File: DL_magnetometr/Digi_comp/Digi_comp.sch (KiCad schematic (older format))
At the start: 30 parts, among them J1 USB_B_Micro, U1 AP7331-WG-7, U2 74AHCT1G125, U3 JST-PHR-2, U4 AZ4558CM, U5 AZ4558CM

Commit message: Add files via upload
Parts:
- added C10, C7, C8, C9: 100n, Capacitor_SMD:C_0402_1005Metric, symbol Device:C
- added C11: 8.2p, Capacitor_SMD:C_0402_1005Metric, symbol Device:C
- added C12, C13: 1.8p, symbol Device:C
- added C14: 0.1u, Capacitor_SMD:C_0402_1005Metric, symbol Device:C
- added C15, C16: 1u, symbol Device:C
- added C4: 4.7u, symbol Device:C
- added L1: 3.3n, symbol Device:L
- added Y1: 32.768k, symbol Device:Crystal
- added Y2: 16M/32M, symbol Device:Crystal
- B1: renamed from B?; symbol RF_Bluetooth:QN908x -> Digi_comp-rescue:QN908x-RF_Bluetooth
- S1: renamed from S?; symbol Sensor:HMC5883L -> Digi_comp-rescue:HMC5883L-Sensor
- U1: symbol Regulator_Linear:AP7331-WG-7 -> Digi_comp-rescue:AP7331-WG-7-Regulator_Linear
- U3: symbol Connector:JST-PHR-2 -> Digi_comp-rescue:JST-PHR-2-Connector
- U4, U5: symbol Amplifier_Audio:AZ4558CM -> Digi_comp-rescue:AZ4558CM-Amplifier_Audio
- U6: renamed from U?; symbol Regulator_Linear:AP7331-WG-7 -> Digi_comp-rescue:AP7331-WG-7-Regulator_Linear
- gave numbers to parts that had none: 1
- renumbered RG to RG1, R_SHUNT to R_SHUNT1
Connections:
- net labels added: CHIP_MODE, ISP_RXD, ISP_TXD, RSTN, SW_CLK, SW_DIO
- wire segments 113 -> 172
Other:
- note added: "#ToDo: Antenna"
- note added: "#Todo: Fix RESET bug\n"
- moved on the sheet: R11, R12, R13

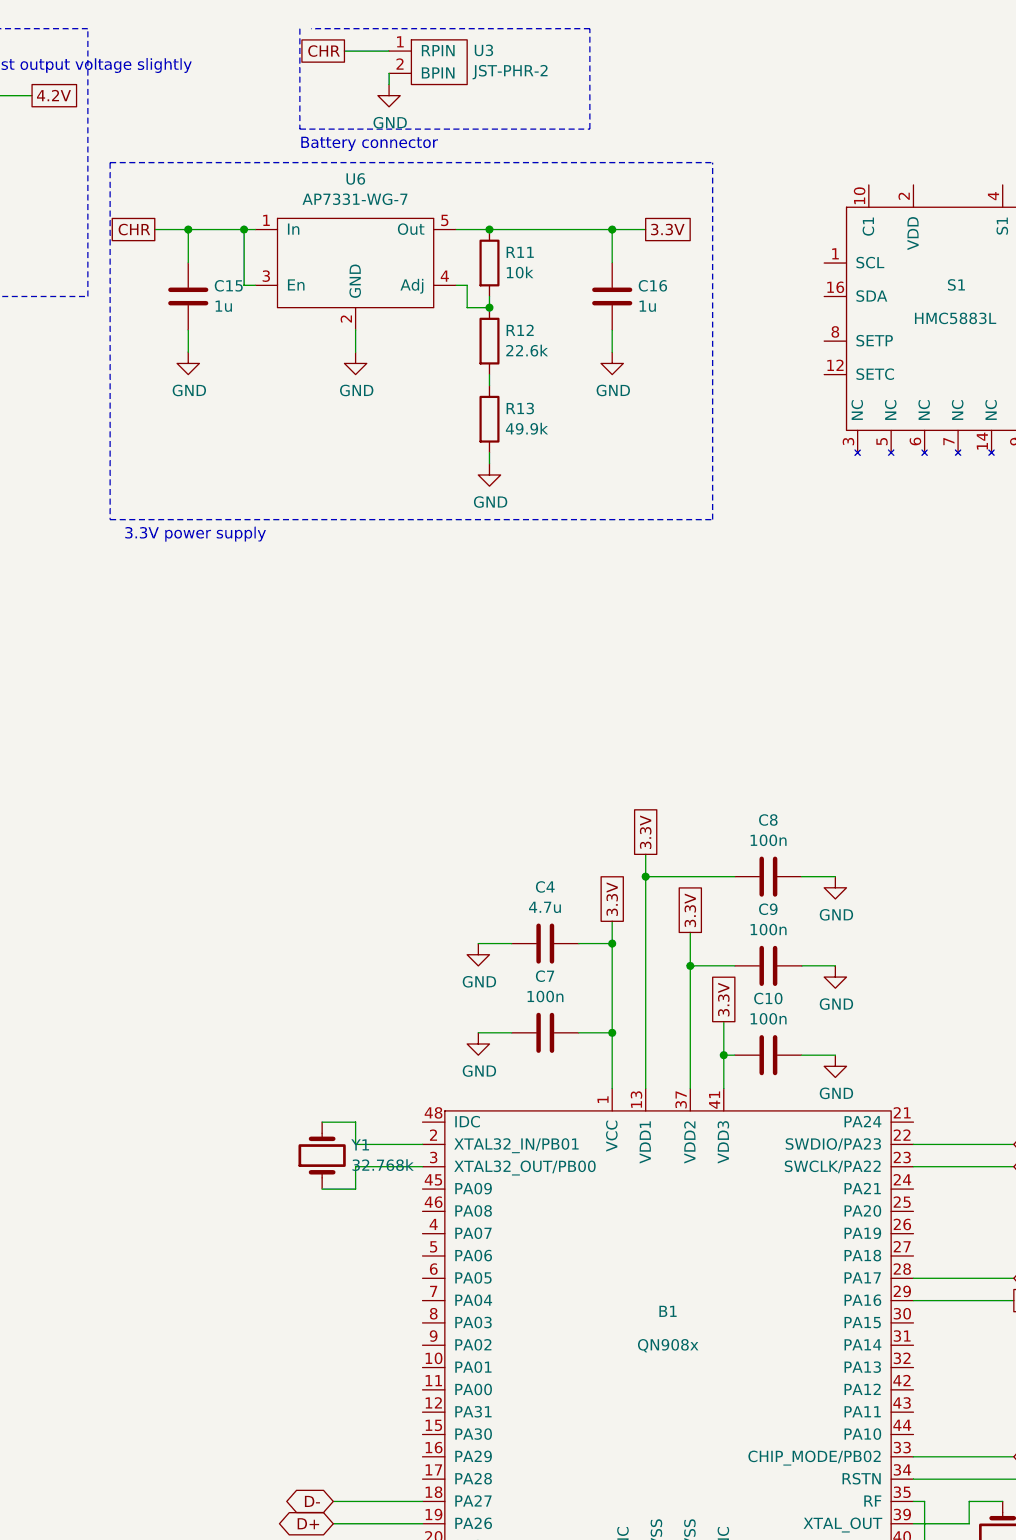
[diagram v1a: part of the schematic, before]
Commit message: Modified scheme
Now utilising on-chip DC-DC converter for lower power consumption. Added overcurrent protection fuses.
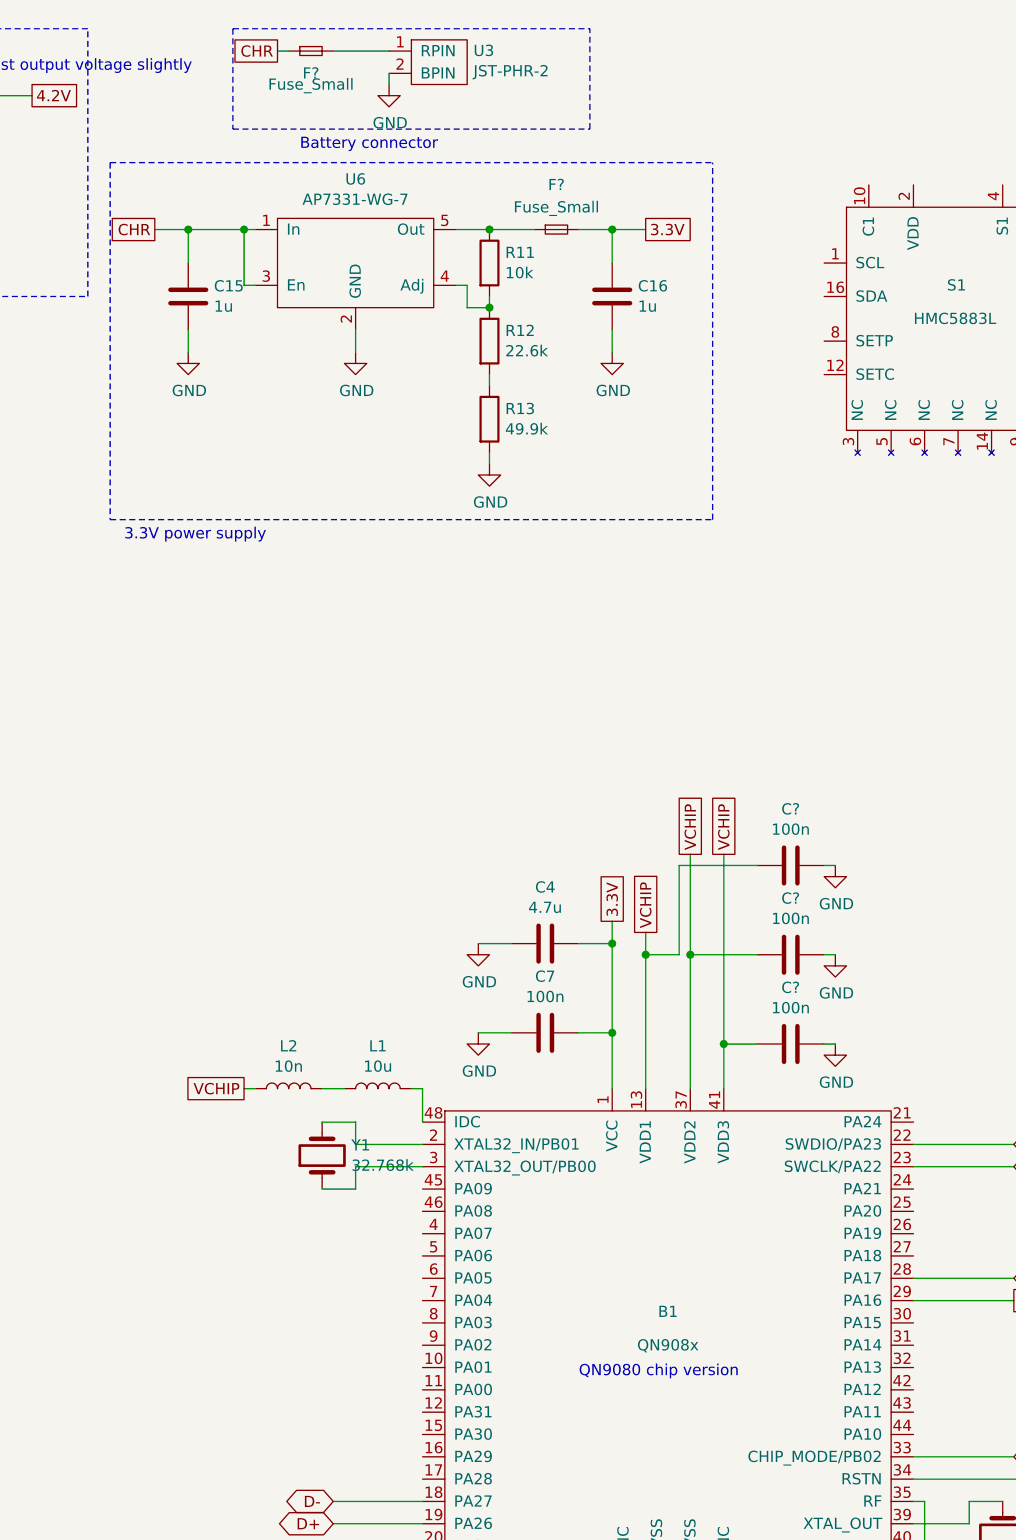
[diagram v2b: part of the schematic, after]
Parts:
- removed C10, C8, C9: 100n, Capacitor_SMD:C_0402_1005Metric, symbol Device:C
- added C? (x3): 100n, Capacitor_SMD:C_0402_1005Metric, symbol Device:C
- added F? (x2): Fuse_Small, symbol Device:Fuse_Small
- added L1: 10u, symbol Device:L
- added L2: 10n, symbol Device:L
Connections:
- net 3.3V: now also F?.2; no longer B1.13 (VDD1), B1.37 (VDD2), B1.41 (VDD3), R11.1, U6.5 (Out)
- net CHR: now also F?.1; no longer U3.1 (RPIN)
- net GND: now also C?.1, C?.1, C?.1
- net at B1.48 (IDC): now also L1.2
- new net: F?.2, U3.1 (RPIN)
- new net: F?.1, R11.1, U6.5 (Out)
- new net: L1.1, L2.2
- new net VCHIP: B1.13 (VDD1), B1.37 (VDD2), B1.41 (VDD3), C?.2, C?.2, C?.2, L2.1
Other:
- note added: "QN9080 chip version"
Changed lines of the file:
@@
 Text GLabel 2200 4900 2    50   UnSpc ~ 0
 BAT
-Wire Wire Line
-	6500 700  6300 700
 $Comp
 L Digi_comp-rescue:AZ4558CM-Amplifier_Audio U4
@@
 Text GLabel 1600 4900 0    50   UnSpc ~ 0
 CHR
-Text GLabel 6300 700  0    50   UnSpc ~ 0
+Text GLabel 6000 700  0    50   UnSpc ~ 0
 CHR
 Text Notes 4050 800  0    50   ~ 0
@@
 $EndComp
 Wire Notes Line
-	6100 600  6100 1050
-Wire Notes Line
-	6100 1050 7400 1050
+	5800 600  5800 1050
 Wire Notes Line
 	7400 1050 7400 600
-Wire Notes Line
-	7400 600  6150 600
 Text Notes 6100 1150 0    50   ~ 0
 Battery connector
@@
 Text GLabel 7650 1500 2    50   UnSpc ~ 0
 3.3V
-Connection ~ 6950 1500
 Wire Wire Line
 	1450 2750 1100 2750
@@
 Wire Wire Line
 	6900 4700 7050 4700
-$Comp
-L Device:C C10
-U 1 1 5FDD7B44
-P 8200 5200
-F 0 "C10" V 7948 5200 50  0000 C CNN
-F 1 "100n" V 8039 5200 50  0000 C CNN
-F 2 "Capacitor_SMD:C_0402_1005Metric" H 8238 5050 50  0001 C CNN
-F 3 "~" H 8200 5200 50  0001 C CNN
-	1    8200 5200
-	0    1    1    0
-$EndComp
-$Comp
-L power:GND #PWR03
-U 1 1 5FDD8027
-P 8500 5200
-F 0 "#PWR03" H 8500 4950 50  0001 C CNN
-F 1 "GND" H 8505 5027 50  0000 C CNN
-F 2 "" H 8500 5200 50  0001 C CNN
-F 3 "" H 8500 5200 50  0001 C CNN
-	1    8500 5200
-	1    0    0    -1
-$EndComp
-$Comp
-L Device:C C9
-U 1 1 5FDD8471
-P 8200 4800
-F 0 "C9" V 7948 4800 50  0000 C CNN
-F 1 "100n" V 8039 4800 50  0000 C CNN
-F 2 "Capacitor_SMD:C_0402_1005Metric" H 8238 4650 50  0001 C CNN
-F 3 "~" H 8200 4800 50  0001 C CNN
-	1    8200 4800
-	0    1    1    0
-$EndComp
-$Comp
-L power:GND #PWR02
-U 1 1 5FDD87FC
-P 8500 4800
-F 0 "#PWR02" H 8500 4550 50  0001 C CNN
-F 1 "GND" H 8505 4627 50  0000 C CNN
-F 2 "" H 8500 4800 50  0001 C CNN
-F 3 "" H 8500 4800 50  0001 C CNN
-	1    8500 4800
-	1    0    0    -1
-$EndComp
-Text GLabel 8000 5050 1    50   UnSpc ~ 0
-3.3V
-Text GLabel 7850 4650 1    50   UnSpc ~ 0
-3.3V
-$Comp
-L Device:C C8
-U 1 1 5FDDA27E
-P 8200 4400
-F 0 "C8" V 7948 4400 50  0000 C CNN
-F 1 "100n" V 8039 4400 50  0000 C CNN
-F 2 "Capacitor_SMD:C_0402_1005Metric" H 8238 4250 50  0001 C CNN
-F 3 "~" H 8200 4400 50  0001 C CNN
-	1    8200 4400
-	0    1    1    0
-$EndComp
-$Comp
-L power:GND #PWR01
-U 1 1 5FDDAA82
-P 8500 4400
-F 0 "#PWR01" H 8500 4150 50  0001 C CNN
-F 1 "GND" H 8505 4227 50  0000 C CNN
-F 2 "" H 8500 4400 50  0001 C CNN
-F 3 "" H 8500 4400 50  0001 C CNN
-	1    8500 4400
-	1    0    0    -1
-$EndComp
-Text GLabel 7650 4300 1    50   UnSpc ~ 0
-3.3V
-Wire Wire Line
-	8350 4400 8500 4400
-Wire Wire Line
-	8350 4800 8500 4800
-Wire Wire Line
-	7650 4300 7650 4400
-Wire Wire Line
-	7850 4650 7850 4800
-Wire Wire Line
-	7650 4400 8050 4400
-Wire Wire Line
-	7850 4800 8050 4800
-Wire Wire Line
-	8050 5200 8000 5200
-Wire Wire Line
-	8000 5200 8000 5050
-Wire Wire Line
-	8000 5200 8000 5350
-Connection ~ 8000 5200
-Wire Wire Line
-	8350 5200 8500 5200
 Text GLabel 9300 6300 2    50   Output ~ 0
 ISP_TXD
@@
 Text GLabel 6250 7200 0    50   BiDi ~ 0
 D-
-Wire Wire Line
-	7850 5350 7850 4800
-Connection ~ 7850 4800
-Wire Wire Line
-	7650 5350 7650 4400
-Connection ~ 7650 4400
 Text Notes 8750 8700 0    50   ~ 0
 #ToDo: Antenna
@@
 	7500 1500 7650 1500
 Wire Wire Line
-	6950 1500 7500 1500
-Connection ~ 7500 1500
-Wire Wire Line
 	5450 1500 5600 1500
 Wire Wire Line
@@
 Wire Notes Line
 	5250 2800 7950 2800
+$Comp
+L Device:Fuse_Small F?
+U 1 1 5FD84E19
+P 6150 700
+F 0 "F?" H 6150 600 50  0000 C CNN
+F 1 "Fuse_Small" H 6150 550 50  0000 C CNN
+F 2 "" H 6150 700 50  0001 C CNN
+F 3 "~" H 6150 700 50  0001 C CNN
+	1    6150 700
+	1    0    0    -1
+$EndComp
+Wire Wire Line
+	6250 700  6500 700
+Wire Wire Line
+	6050 700  6000 700
+Wire Notes Line
+	5800 1050 7400 1050
+Wire Notes Line
+	5800 600  7400 600
+$Comp
+L Device:Fuse_Small F?
+U 1 1 5FDB2E3B
+P 7250 1500
+F 0 "F?" H 7250 1700 50  0000 C CNN
+F 1 "Fuse_Small" H 7250 1600 50  0000 C CNN
+F 2 "" H 7250 1500 50  0001 C CNN
+F 3 "~" H 7250 1500 50  0001 C CNN
+	1    7250 1500
+	1    0    0    -1
+$EndComp
+Wire Wire Line
+	6950 1500 7150 1500
+Connection ~ 6950 1500
+Wire Wire Line
+	7350 1500 7500 1500
+Connection ~ 7500 1500
+$Comp
+L Device:L L1
+U 1 1 5FDC3994
+P 6450 5350
+F 0 "L1" V 6640 5350 50  0000 C CNN
+F 1 "10u" V 6549 5350 50  0000 C CNN
+F 2 "" H 6450 5350 50  0001 C CNN
+F 3 "~" H 6450 5350 50  0001 C CNN
+	1    6450 5350
+	0    -1   -1   0
+$EndComp
+$Comp
+L Device:L L2
+U 1 1 5FDC45C3
+P 6050 5350
+F 0 "L2" V 6240 5350 50  0000 C CNN
+F 1 "10n" V 6149 5350 50  0000 C CNN
+F 2 "" H 6050 5350 50  0001 C CNN
+F 3 "~" H 6050 5350 50  0001 C CNN
+	1    6050 5350
+	0    -1   -1   0
+$EndComp
+Wire Wire Line
+	6650 5500 6650 5350
+Wire Wire Line
+	6650 5350 6600 5350
+Wire Wire Line
+	6300 5350 6200 5350
+Text GLabel 5850 5350 0    50   UnSpc ~ 0
+VCHIP
+Wire Wire Line
+	5900 5350 5850 5350
+Text GLabel 7650 4650 1    50   UnSpc ~ 0
+VCHIP
+$Comp
+L Device:C C?
+U 1 1 5FDDA059
+P 8300 4750
+F 0 "C?" V 8048 4750 50  0000 C CNN
+F 1 "100n" V 8139 4750 50  0000 C CNN
+F 2 "Capacitor_SMD:C_0402_1005Metric" H 8338 4600 50  0001 C CNN
+F 3 "~" H 8300 4750 50  0001 C CNN
+	1    8300 4750
+	0    1    1    0
+$EndComp
+$Comp
+L Device:C C?
+U 1 1 5FDDAC74
+P 8300 5150
+F 0 "C?" V 8048 5150 50  0000 C CNN
+F 1 "100n" V 8139 5150 50  0000 C CNN
+F 2 "Capacitor_SMD:C_0402_1005Metric" H 8338 5000 50  0001 C CNN
+F 3 "~" H 8300 5150 50  0001 C CNN
+	1    8300 5150
+	0    1    1    0
+$EndComp
+$Comp
+L Device:C C?
+U 1 1 5FDDB25A
+P 8300 4350
+F 0 "C?" V 8048 4350 50  0000 C CNN
+F 1 "100n" V 8139 4350 50  0000 C CNN
+F 2 "Capacitor_SMD:C_0402_1005Metric" H 8338 4200 50  0001 C CNN
+F 3 "~" H 8300 4350 50  0001 C CNN
+	1    8300 4350
+	0    1    1    0
+$EndComp
+Wire Wire Line
+	7650 4650 7650 4750
+Wire Wire Line
+	7650 4750 7800 4750
+Wire Wire Line
+	7800 4750 7800 4350
+Wire Wire Line
+	7800 4350 8150 4350
+Connection ~ 7650 4750
+Wire Wire Line
+	7650 4750 7650 5350
+Text GLabel 7850 4300 1    50   UnSpc ~ 0
+VCHIP
+Wire Wire Line
+	7850 4300 7850 4750
+Wire Wire Line
+	7850 4750 8150 4750
+Connection ~ 7850 4750
+Wire Wire Line
+	7850 4750 7850 5350
+Text GLabel 8000 4300 1    50   UnSpc ~ 0
+VCHIP
+Wire Wire Line
+	8000 4300 8000 5150
+Wire Wire Line
+	8150 5150 8000 5150
+Connection ~ 8000 5150
+Wire Wire Line
+	8000 5150 8000 5350
+$Comp
+L power:GND #PWR?
+U 1 1 5FE096DE
+P 8500 5150
+F 0 "#PWR?" H 8500 4900 50  0001 C CNN
+F 1 "GND" H 8505 4977 50  0000 C CNN
+F 2 "" H 8500 5150 50  0001 C CNN
+F 3 "" H 8500 5150 50  0001 C CNN
+	1    8500 5150
+	1    0    0    -1
+$EndComp
+Wire Wire Line
+	8500 5150 8450 5150
+$Comp
+L power:GND #PWR?
+U 1 1 5FE11A43
+P 8500 4750
+F 0 "#PWR?" H 8500 4500 50  0001 C CNN
+F 1 "GND" H 8505 4577 50  0000 C CNN
+F 2 "" H 8500 4750 50  0001 C CNN
+F 3 "" H 8500 4750 50  0001 C CNN
+	1    8500 4750
+	1    0    0    -1
+$EndComp
+Wire Wire Line
+	8500 4750 8450 4750
+$Comp
+L power:GND #PWR?
+U 1 1 5FE1A0CD
+P 8500 4350
+F 0 "#PWR?" H 8500 4100 50  0001 C CNN
+F 1 "GND" H 8505 4177 50  0000 C CNN
+F 2 "" H 8500 4350 50  0001 C CNN
+F 3 "" H 8500 4350 50  0001 C CNN
+	1    8500 4350
+	1    0    0    -1
+$EndComp
+Wire Wire Line
+	8500 4350 8450 4350
+Text Notes 7350 6650 0    50   ~ 0
+QN9080 chip version
 $EndSCHEMATC

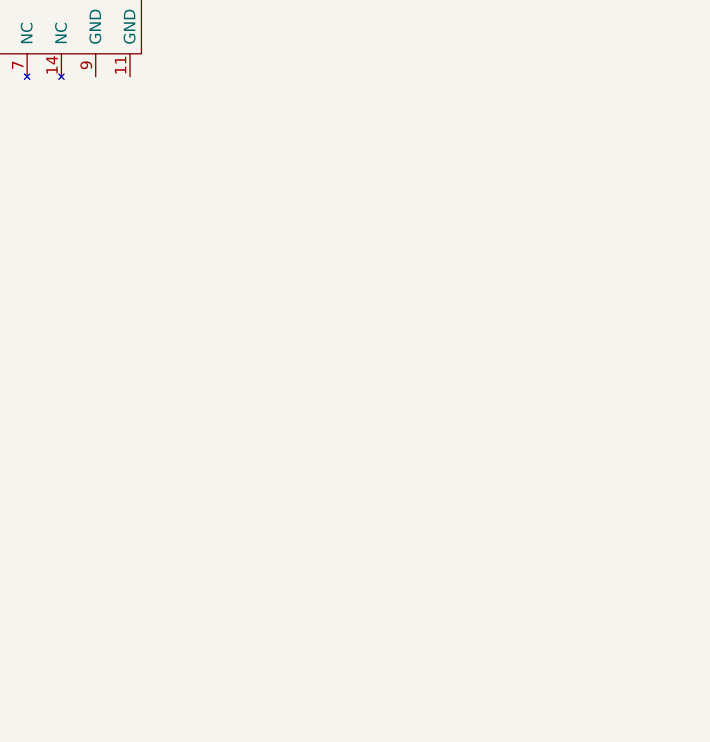
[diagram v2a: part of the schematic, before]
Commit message: Added new symbol
Added symbol of the PK20DX128VFM5 component (required for programming the MCU)
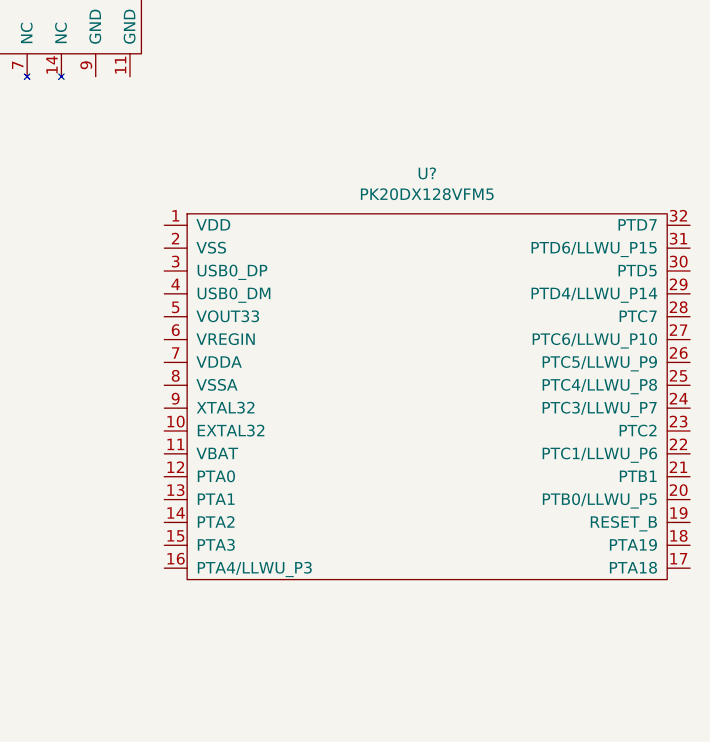
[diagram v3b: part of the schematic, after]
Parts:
- added U?: PK20DX128VFM5, symbol CPU:PK20DX128VFM5
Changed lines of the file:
@@
 Text Notes 7350 6650 0    50   ~ 0
 QN9080 chip version
+$Comp
+L CPU:PK20DX128VFM5 U?
+U 1 1 5FDA32A7
+P 10800 3600
+F 0 "U?" H 10800 4275 50  0000 C CNN
+F 1 "PK20DX128VFM5" H 10800 4184 50  0000 C CNN
+F 2 "" H 10600 3600 50  0001 C CNN
+F 3 "" H 10600 3600 50  0001 C CNN
+	1    10800 3600
+	1    0    0    -1
+$EndComp
 $EndSCHEMATC
